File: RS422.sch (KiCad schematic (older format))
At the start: 6 parts, among them J9 RJ45_LED

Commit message: updated RS422
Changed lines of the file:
@@
 F4 "MODE" I R 5850 1500 50
 F5 "VCC" I R 5850 1400 50
-F6 "OUT" I R 5850 1650 50
+F6 "DATA" B R 5850 1650 50
 $EndSheet
 Text HLabel 5950 1650 2    50   Input ~ 0
@@
 F4 "MODE" I R 5850 5300 50
 F5 "VCC" I R 5850 4900 50
-F6 "OUT" I R 5850 5150 50
+F6 "DATA" B R 5850 5150 50
 $EndSheet
 Wire Wire Line
@@
 F4 "MODE" I R 5850 7000 50
 F5 "VCC" I R 5850 6600 50
-F6 "OUT" I R 5850 6850 50
+F6 "DATA" B R 5850 6850 50
 $EndSheet
 Wire Wire Line
@@
 Wire Wire Line
 	3600 1800 5150 1800
-$Sheet
-S 5150 3000 700  600
-U 607938CE
-F0 "RS485Tranceiver2" 50
-F1 "RS485Tranceiver.sch" 50
-F2 "A_in" I L 5150 3100 50
-F3 "B_in" I L 5150 3500 50
-F4 "MODE" I R 5850 3500 50
-F5 "VCC" I R 5850 3100 50
-F6 "OUT" I R 5850 3350 50
-$EndSheet
 $Comp
 L power:GND #PWR092
@@
 Wire Wire Line
 	2400 3800 2200 3800
+$Sheet
+S 5150 3000 700  600
+U 607938CE
+F0 "RS485Tranceiver2" 50
+F1 "RS485Tranceiver.sch" 50
+F2 "A_in" I L 5150 3100 50
+F3 "B_in" I L 5150 3500 50
+F4 "MODE" I R 5850 3500 50
+F5 "VCC" I R 5850 3100 50
+F6 "DATA" B R 5850 3350 50
+$EndSheet
 $EndSCHEMATC

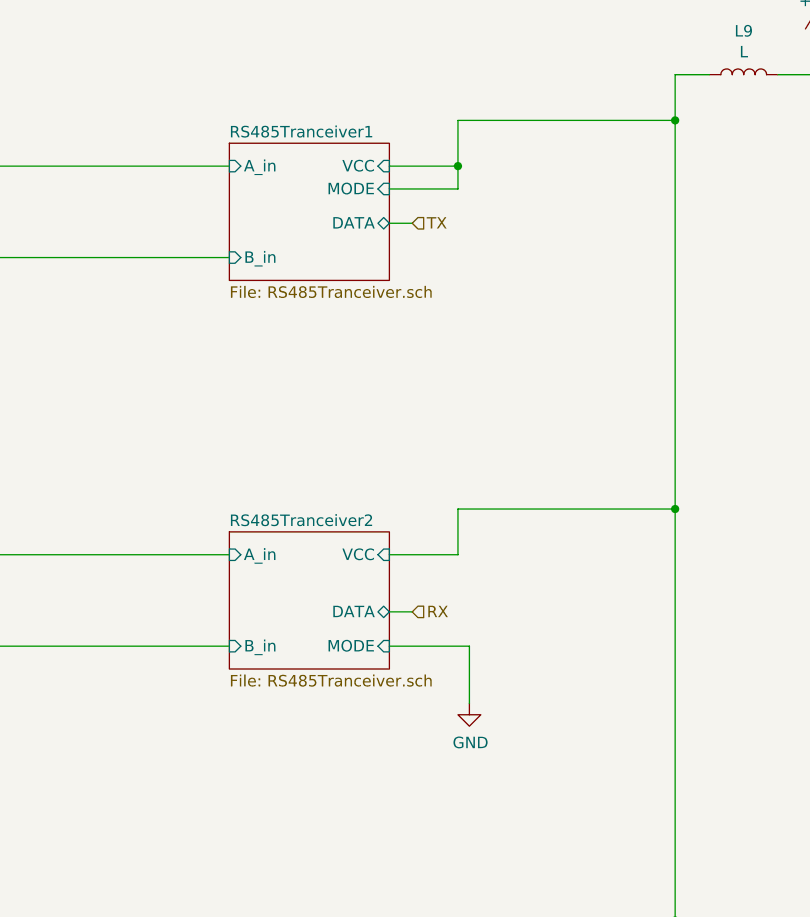
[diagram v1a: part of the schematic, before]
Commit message: rx tx fix, filter mirrored
switched rx/tx signals
filters were mirrored
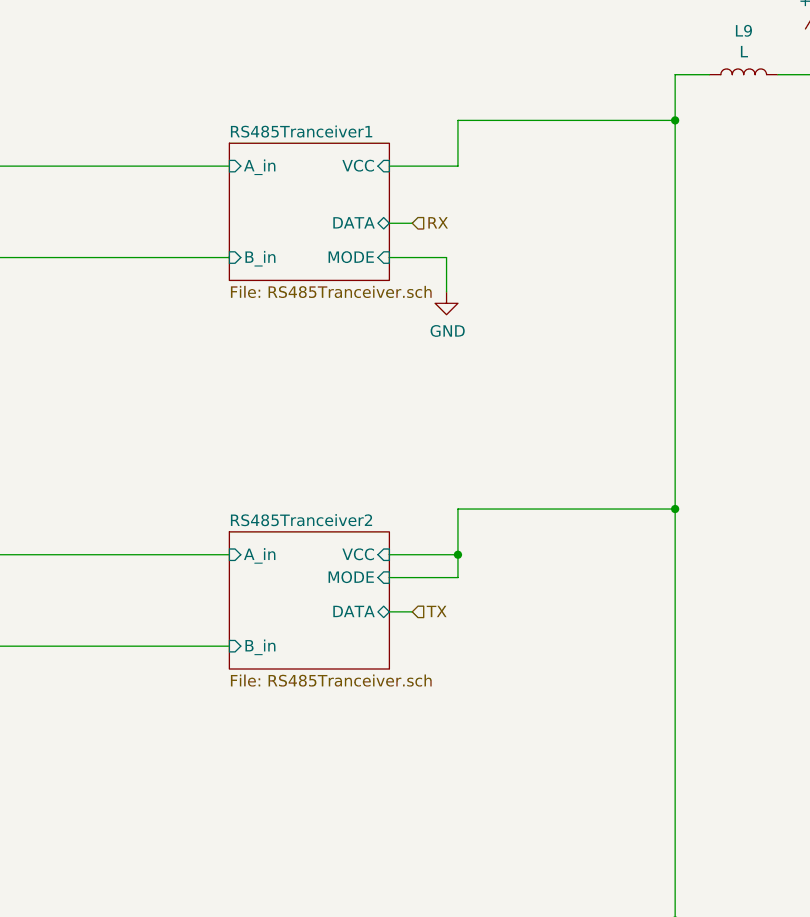
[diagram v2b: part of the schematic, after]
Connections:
- net RS485Tranceiver1/MODE renamed RS485Tranceiver1/VCC
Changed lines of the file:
@@
 $Descr A4 11693 8268
 encoding utf-8
-Sheet 13 17
+Sheet 13 21
 Title ""
 Date ""
@@
 Wire Wire Line
 	3450 4900 3450 3050
-$Sheet
-S 5150 1300 700  600
-U 60727BD1
-F0 "RS485Tranceiver1" 50
-F1 "RS485Tranceiver.sch" 50
-F2 "A_in" I L 5150 1400 50
-F3 "B_in" I L 5150 1800 50
-F4 "MODE" I R 5850 1500 50
-F5 "VCC" I R 5850 1400 50
-F6 "DATA" B R 5850 1650 50
-$EndSheet
-Text HLabel 5950 1650 2    50   Input ~ 0
+Text HLabel 5950 3350 2    50   Input ~ 0
 TX
 Wire Wire Line
@@
 Wire Wire Line
 	6150 1200 7100 1200
-Wire Wire Line
-	5850 1500 6150 1500
-Wire Wire Line
-	6150 1500 6150 1400
-Connection ~ 6150 1400
 Text HLabel 5950 6850 2    50   Input ~ 0
 PTT2
 Text HLabel 5950 5150 2    50   Input ~ 0
 PTT1
-Text HLabel 5950 3350 2    50   Input ~ 0
+Text HLabel 5950 1650 2    50   Input ~ 0
 RX
 Wire Wire Line
@@
 	3600 1800 5150 1800
 $Comp
-L power:GND #PWR092
-U 1 1 607AD833
-P 6200 3750
-F 0 "#PWR092" H 6200 3500 50  0001 C CNN
-F 1 "GND" H 6205 3577 50  0000 C CNN
-F 2 "" H 6200 3750 50  0001 C CNN
-F 3 "" H 6200 3750 50  0001 C CNN
-	1    6200 3750
-	1    0    0    -1
-$EndComp
-Wire Wire Line
-	6200 3750 6200 3500
-Wire Wire Line
-	6200 3500 5850 3500
-$Comp
 L power:GND #PWR0102
 U 1 1 607B0400
@@
 F2 "A_in" I L 5150 3100 50
 F3 "B_in" I L 5150 3500 50
-F4 "MODE" I R 5850 3500 50
+F4 "MODE" I R 5850 3200 50
 F5 "VCC" I R 5850 3100 50
 F6 "DATA" B R 5850 3350 50
 $EndSheet
+$Sheet
+S 5150 1300 700  600
+U 60727BD1
+F0 "RS485Tranceiver1" 50
+F1 "RS485Tranceiver.sch" 50
+F2 "A_in" I L 5150 1400 50
+F3 "B_in" I L 5150 1800 50
+F4 "MODE" I R 5850 1800 50
+F5 "VCC" I R 5850 1400 50
+F6 "DATA" B R 5850 1650 50
+$EndSheet
+$Comp
+L power:GND #PWR092
+U 1 1 60908821
+P 6100 1950
+F 0 "#PWR092" H 6100 1700 50  0001 C CNN
+F 1 "GND" H 6105 1777 50  0000 C CNN
+F 2 "" H 6100 1950 50  0001 C CNN
+F 3 "" H 6100 1950 50  0001 C CNN
+	1    6100 1950
+	1    0    0    -1
+$EndComp
+Wire Wire Line
+	5850 1800 6100 1800
+Wire Wire Line
+	6100 1800 6100 1950
+Wire Wire Line
+	5850 3200 6150 3200
+Wire Wire Line
+	6150 3200 6150 3100
+Connection ~ 6150 3100
 $EndSCHEMATC

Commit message: uart rx tx reversed
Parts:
- J9: symbol stmbl:RJ45_LED -> AR2ISS_AntCTL_HW-rescue:RJ45_LED-stmbl
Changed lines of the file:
@@
 	7100 4700 7100 6400
 $Comp
-L stmbl:RJ45_LED J9
+L AR2ISS_AntCTL_HW-rescue:RJ45_LED-stmbl J9
 U 1 1 607241AA
 P 2400 3150
+AR Path="/607241AA" Ref="J9"  Part="1"
+AR Path="/6072829D/607241AA" Ref="J9"  Part="1"
 F 0 "J9" V 1775 3150 50  0000 C CNN
 F 1 "RJ45_LED" V 1866 3150 50  0000 C CNN
